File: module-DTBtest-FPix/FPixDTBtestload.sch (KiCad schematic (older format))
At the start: 11 parts, among them J1 CONN-SMK20, P15 RTD+, P16 RTD-

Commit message: Cleaned up the schematic, recovered from a non-present rescue library. Exported the netlist
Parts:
- R1, R2, R3, R4, R5, R6, R7: symbol R-RESCUE-FPix2DTB_90deg_up -> R
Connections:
- wire segments 62 -> 72
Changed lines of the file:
@@
 EESchema Schematic File Version 2
-LIBS:FPix2DTB_90deg_up-rescue
 LIBS:power
 LIBS:device
@@
 LIBS:contrib
 LIBS:valves
-LIBS:conn-scsi68
 LIBS:FPixDTBtestload-cache
 EELAYER 25 0
@@
 NoConn ~ 6400 4750
 $Comp
-L R-RESCUE-FPix2DTB_90deg_up R2
+L R R2
 U 1 1 526C35D1
 P 7750 2000
@@
 $EndComp
 $Comp
-L R-RESCUE-FPix2DTB_90deg_up R1
+L R R1
 U 1 1 526C35EF
 P 7750 1350
@@
 Jumper will short accross \nextra calibration resistor
 $Comp
-L R-RESCUE-FPix2DTB_90deg_up R3
+L R R3
 U 1 1 558082B2
 P 8100 4650
@@
 $EndComp
 $Comp
-L R-RESCUE-FPix2DTB_90deg_up R6
+L R R6
 U 1 1 5582CB84
 P 7700 5550
@@
 Connection ~ 8950 1650
 Connection ~ 8950 2300
-Wire Wire Line
-	7750 2300 7750 2250
 Connection ~ 8700 2300
 Connection ~ 7750 2300
@@
 	6400 4550 6650 4550
 Wire Wire Line
-	6400 4650 7850 4650
+	6400 4650 7950 4650
 Wire Wire Line
 	6400 4850 6650 4850
@@
 	7150 1100 7750 1100
 Wire Wire Line
-	7750 1600 7750 1750
-Wire Wire Line
 	7150 2300 8700 2300
 Wire Wire Line
@@
 	5650 5800 8100 5800
 $Comp
-L R-RESCUE-FPix2DTB_90deg_up R4
+L R R4
 U 1 1 5582CE8F
 P 7700 3650
@@
 Connection ~ 5650 3400
 $Comp
-L R-RESCUE-FPix2DTB_90deg_up R5
+L R R5
 U 1 1 5582D226
 P 8100 3650
@@
 Connection ~ 7700 3900
 $Comp
-L R-RESCUE-FPix2DTB_90deg_up R7
+L R R7
 U 1 1 5582D3F6
 P 8100 5550
@@
 	8350 6000 5650 6000
 Connection ~ 5650 6000
+Wire Wire Line
+	7750 1100 7750 1200
+Wire Wire Line
+	7750 1500 7750 1850
+Wire Wire Line
+	7750 2300 7750 2150
+Wire Wire Line
+	7700 3500 7700 3400
+Wire Wire Line
+	8100 3400 8100 3500
+Wire Wire Line
+	7700 3900 7700 3800
+Wire Wire Line
+	8100 3900 8100 3800
+Wire Wire Line
+	7700 5400 7700 5300
+Wire Wire Line
+	8100 5300 8100 5400
+Wire Wire Line
+	7700 5800 7700 5700
+Wire Wire Line
+	8100 5800 8100 5700
+Wire Wire Line
+	8250 4650 8350 4650
 $EndSCHEMATC

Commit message: Still working on getting the netlist operational
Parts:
- JP1: footprint Short_Link -> PIN_ARRAY_2X1
- R1, R2: footprint SM0603 -> Resistors_SMD:R_0603_HandSoldering
- R3: footprint (none) -> Resistors_SMD:R_Caddock_USF371
- R4, R5, R6, R7: footprint (none) -> Resistors_SMD:R_2512_HandSoldering
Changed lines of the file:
@@
 F 0 "R2" V 7830 2000 40  0000 C CNN
 F 1 "10k 0.1%" V 7757 2001 40  0000 C CNN
-F 2 "SM0603" V 7680 2000 30  0000 C CNN
+F 2 "Resistors_SMD:R_0603_HandSoldering" V 7680 2000 30  0000 C CNN
 F 3 "" H 7750 2000 30  0000 C CNN
 	1    7750 2000
@@
 F 0 "R1" V 7830 1350 40  0000 C CNN
 F 1 "10k 0.1%" V 7757 1351 40  0000 C CNN
-F 2 "SM0603" V 7680 1350 30  0000 C CNN
+F 2 "Resistors_SMD:R_0603_HandSoldering" V 7680 1350 30  0000 C CNN
 F 3 "" H 7750 1350 30  0000 C CNN
 	1    7750 1350
@@
 F 0 "JP1" H 8700 2150 60  0000 C CNN
 F 1 "JUMPER" H 8700 1920 40  0000 C CNN
-F 2 "Short_Link" H 8950 1800 60  0000 R CNN
+F 2 "PIN_ARRAY_2X1" H 8950 1800 60  0000 R CNN
 F 3 "" H 8700 2000 60  0000 C CNN
 	1    8700 2000
@@
 F 0 "R3" V 8180 4650 50  0000 C CNN
 F 1 "25 MEG" V 8107 4651 50  0000 C CNN
-F 2 "" V 8030 4650 30  0000 C CNN
+F 2 "Resistors_SMD:R_Caddock_USF371" V 8030 4650 30  0000 C CNN
 F 3 "" H 8100 4650 30  0000 C CNN
 	1    8100 4650
@@
 F 0 "R6" V 7780 5550 50  0000 C CNN
 F 1 "4.8" V 7707 5551 50  0000 C CNN
-F 2 "" V 7630 5550 30  0000 C CNN
+F 2 "Resistors_SMD:R_2512_HandSoldering" V 7630 5550 30  0000 C CNN
 F 3 "" H 7700 5550 30  0000 C CNN
 	1    7700 5550
@@
 F 0 "R4" V 7800 3650 50  0000 C CNN
 F 1 "3.2" V 7707 3651 50  0000 C CNN
-F 2 "" V 7630 3650 30  0000 C CNN
+F 2 "Resistors_SMD:R_2512_HandSoldering" V 7630 3650 30  0000 C CNN
 F 3 "" H 7700 3650 30  0000 C CNN
 	1    7700 3650
 	1    0    0    -1
 $EndComp
-Wire Wire Line
-	5650 3400 8100 3400
 Connection ~ 5650 5800
 Connection ~ 5650 3400
@@
 F 0 "R5" V 8180 3650 50  0000 C CNN
 F 1 "3.2" V 8107 3651 50  0000 C CNN
-F 2 "" V 8030 3650 30  0000 C CNN
+F 2 "Resistors_SMD:R_2512_HandSoldering" V 8030 3650 30  0000 C CNN
 F 3 "" H 8100 3650 30  0000 C CNN
 	1    8100 3650
 	1    0    0    -1
 $EndComp
-Connection ~ 7700 3400
 Connection ~ 7700 3900
 $Comp
@@
 F 0 "R7" V 8180 5550 50  0000 C CNN
 F 1 "4.8" V 8107 5551 50  0000 C CNN
-F 2 "" V 8030 5550 30  0000 C CNN
+F 2 "Resistors_SMD:R_2512_HandSoldering" V 8030 5550 30  0000 C CNN
 F 3 "" H 8100 5550 30  0000 C CNN
 	1    8100 5550
@@
 Wire Wire Line
 	8250 4650 8350 4650
+$Comp
+L GND #PWR?
+U 1 1 5584283A
+P 8500 3400
+F 0 "#PWR?" H 8500 3150 50  0001 C CNN
+F 1 "GND" H 8500 3250 50  0000 C CNN
+F 2 "" H 8500 3400 60  0000 C CNN
+F 3 "" H 8500 3400 60  0000 C CNN
+	1    8500 3400
+	1    0    0    -1
+$EndComp
+Wire Wire Line
+	7700 3400 8500 3400
+Connection ~ 8100 3400
 $EndSCHEMATC

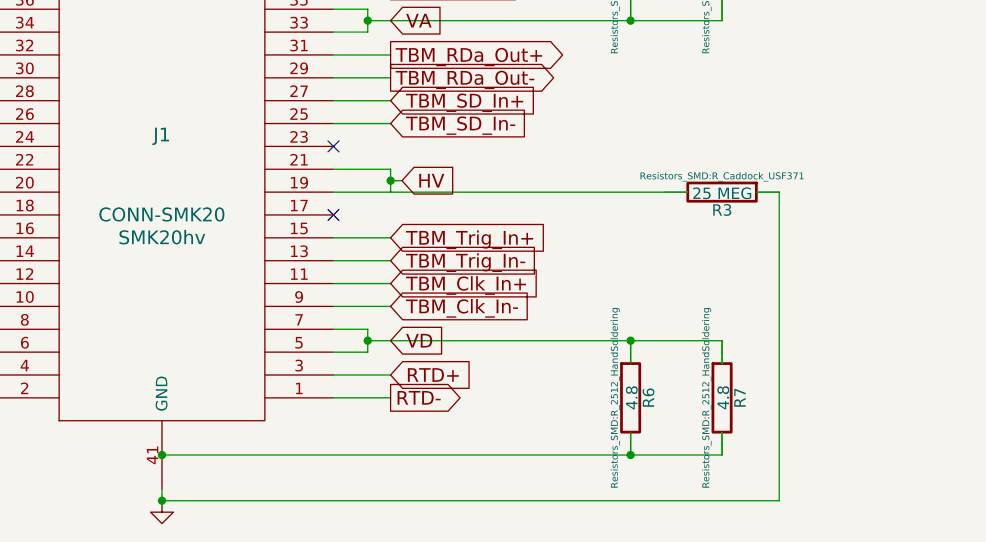
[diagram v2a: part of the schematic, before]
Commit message: Improved grounding
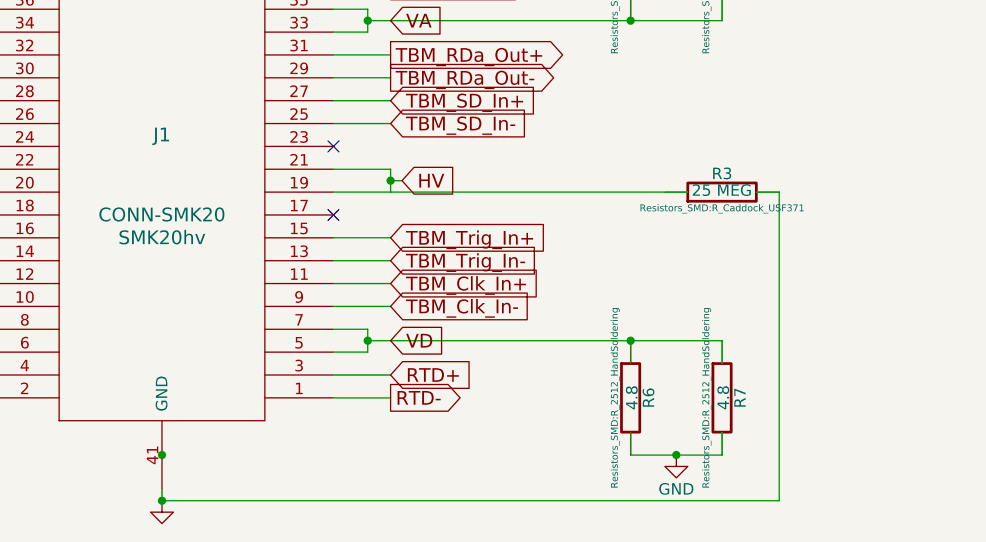
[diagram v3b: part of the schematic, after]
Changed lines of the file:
@@
 F 3 "" H 8100 4650 30  0000 C CNN
 	1    8100 4650
-	0    1    1    0
+	0    -1   -1   0
 $EndComp
 $Comp
@@
 	8700 1700 7750 1700
 Connection ~ 7750 1700
-Wire Wire Line
-	5650 5800 8100 5800
 $Comp
 L R R4
@@
 $EndComp
 Connection ~ 7700 5300
-Connection ~ 7700 5800
 $Comp
 L CONN-SMK20 J1
@@
 	8250 4650 8350 4650
 $Comp
-L GND #PWR?
+L GND #PWR06
 U 1 1 5584283A
 P 8500 3400
-F 0 "#PWR?" H 8500 3150 50  0001 C CNN
+F 0 "#PWR06" H 8500 3150 50  0001 C CNN
 F 1 "GND" H 8500 3250 50  0000 C CNN
 F 2 "" H 8500 3400 60  0000 C CNN
@@
 	7700 3400 8500 3400
 Connection ~ 8100 3400
+$Comp
+L GND #PWR?
+U 1 1 55842B75
+P 7900 5800
+F 0 "#PWR?" H 7900 5550 50  0001 C CNN
+F 1 "GND" H 7900 5650 50  0000 C CNN
+F 2 "" H 7900 5800 60  0000 C CNN
+F 3 "" H 7900 5800 60  0000 C CNN
+	1    7900 5800
+	1    0    0    -1
+$EndComp
+Wire Wire Line
+	7700 5800 8100 5800
+Connection ~ 7900 5800
 $EndSCHEMATC

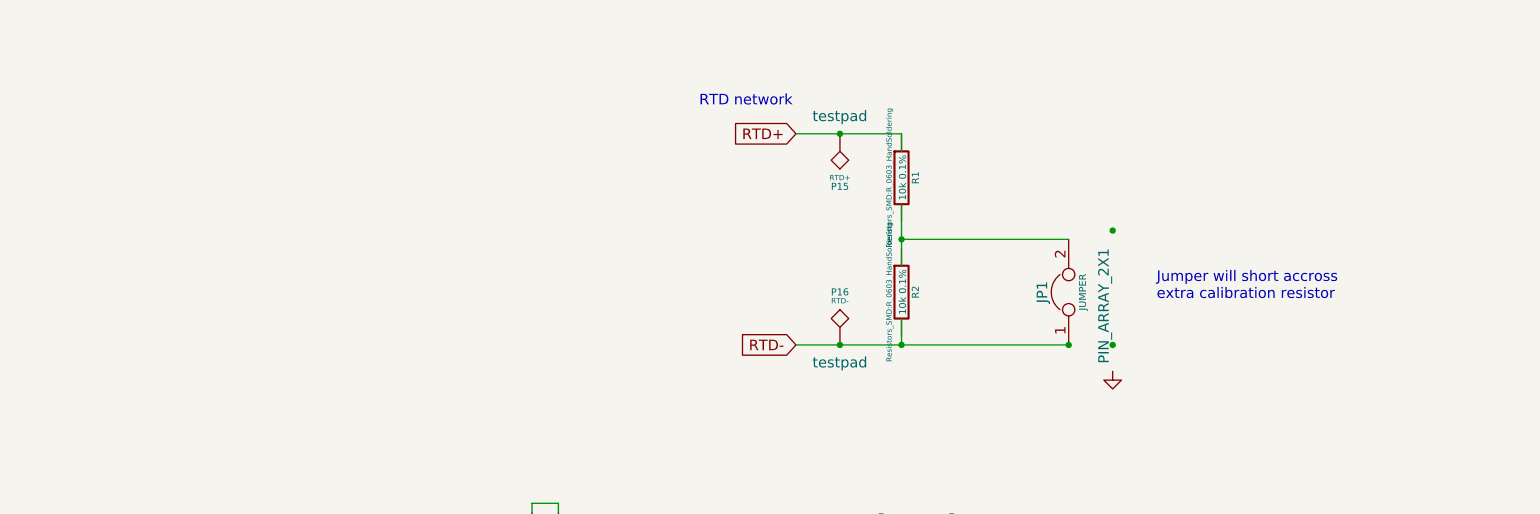
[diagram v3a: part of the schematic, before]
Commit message: Enhanced capabilities of resistor network. Now able to choose 0°C, -25°C and +25°C. Cleaned up GND jumper.
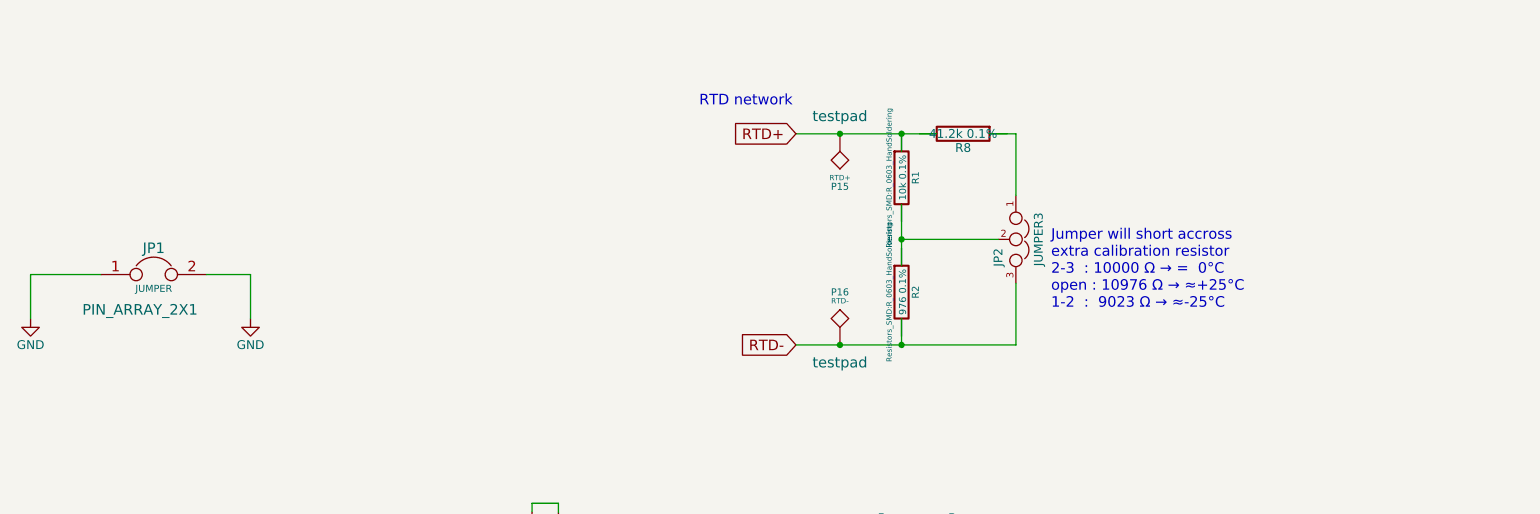
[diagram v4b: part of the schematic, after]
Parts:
- added JP2: JUMPER3, symbol JUMPER3
- added R8: 41.2k 0.1%, symbol R
- R2: value 10k 0.1% -> 976 0.1%
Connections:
- wire segments 72 -> 79
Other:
- note added: "Jumper will short accross \nextra calibration resistor\n2-3 : 10000 Ω → = 0°C\nopen : 10976 Ω → ≈+25°C\n1-2 : 9023 Ω → ≈-25°C"
- note removed: "Jumper will short accross \nextra calibration resistor"
- moved on the sheet: JP1
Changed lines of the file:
@@
 $EndDescr
 $Comp
-L GND #PWR01
+L GND #PWR8
 U 1 1 526C1DE7
 P 13700 -6750
-F 0 "#PWR01" H 13700 -6750 30  0001 C CNN
+F 0 "#PWR8" H 13700 -6750 30  0001 C CNN
 F 1 "GND" H 13700 -6820 30  0001 C CNN
 F 2 "" H 13700 -6750 60  0000 C CNN
@@
 VD
 $Comp
-L GND #PWR02
+L GND #PWR3
 U 1 1 526C1ECD
 P 4150 5650
-F 0 "#PWR02" H 4150 5650 30  0001 C CNN
+F 0 "#PWR3" H 4150 5650 30  0001 C CNN
 F 1 "GND" H 4150 5580 30  0001 C CNN
 F 2 "" H 4150 5650 60  0000 C CNN
@@
 P 7750 2000
 F 0 "R2" V 7830 2000 40  0000 C CNN
-F 1 "10k 0.1%" V 7757 2001 40  0000 C CNN
+F 1 "976 0.1%" V 7757 2001 40  0000 C CNN
 F 2 "Resistors_SMD:R_0603_HandSoldering" V 7680 2000 30  0000 C CNN
 F 3 "" H 7750 2000 30  0000 C CNN
@@
 RTD+
 $Comp
-L GND #PWR03
-U 1 1 526C8E08
-P 8950 2450
-F 0 "#PWR03" H 8950 2450 30  0001 C CNN
-F 1 "GND" H 8950 2380 30  0001 C CNN
-F 2 "" H 8950 2450 60  0000 C CNN
-F 3 "" H 8950 2450 60  0000 C CNN
-	1    8950 2450
-	1    0    0    -1
-$EndComp
-$Comp
 L JUMPER JP1
 U 1 1 526EC969
-P 8700 2000
-F 0 "JP1" H 8700 2150 60  0000 C CNN
-F 1 "JUMPER" H 8700 1920 40  0000 C CNN
-F 2 "PIN_ARRAY_2X1" H 8950 1800 60  0000 R CNN
-F 3 "" H 8700 2000 60  0000 C CNN
-	1    8700 2000
-	0    -1   -1   0
+P 3500 1900
+F 0 "JP1" H 3500 2050 60  0000 C CNN
+F 1 "JUMPER" H 3500 1820 40  0000 C CNN
+F 2 "PIN_ARRAY_2X1" H 3750 1700 60  0000 R CNN
+F 3 "" H 3500 1900 60  0000 C CNN
+	1    3500 1900
+	1    0    0    -1
 $EndComp
 $Comp
@@
 VA
 $Comp
-L GND #PWR04
+L GND #PWR4
 U 1 1 52840820
 P 5650 6000
-F 0 "#PWR04" H 5650 6000 30  0001 C CNN
+F 0 "#PWR4" H 5650 6000 30  0001 C CNN
 F 1 "GND" H 5650 5930 30  0001 C CNN
 F 2 "" H 5650 6000 60  0000 C CNN
@@
 $EndComp
 $Comp
-L GND #PWR05
+L GND #PWR5
 U 1 1 52840925
 P 5800 3250
-F 0 "#PWR05" H 5800 3250 30  0001 C CNN
+F 0 "#PWR5" H 5800 3250 30  0001 C CNN
 F 1 "GND" H 5800 3180 30  0001 C CNN
 F 2 "" H 5800 3250 60  0000 C CNN
@@
 Text Notes 6600 950  0    60   ~ 0
 RTD network
-Text Notes 9200 2050 0    60   ~ 0
-Jumper will short accross \nextra calibration resistor
+Text Notes 8600 2100 0    60   ~ 0
+Jumper will short accross \nextra calibration resistor\n2-3  : 10000 Ω → =  0°C\nopen : 10976 Ω → ≈+25°C\n1-2  :  9023 Ω → ≈-25°C
 $Comp
 L R R3
@@
 	1    0    0    -1
 $EndComp
-Connection ~ 8950 1650
-Connection ~ 8950 2300
-Connection ~ 8700 2300
 Connection ~ 7750 2300
 Connection ~ 7400 1100
@@
 	6400 5550 6650 5550
 Wire Wire Line
-	7150 1100 7750 1100
-Wire Wire Line
-	7150 2300 8700 2300
-Wire Wire Line
-	8700 1700 7750 1700
+	7150 1100 7950 1100
 Connection ~ 7750 1700
 $Comp
@@
 	8250 4650 8350 4650
 $Comp
-L GND #PWR06
+L GND #PWR7
 U 1 1 5584283A
 P 8500 3400
-F 0 "#PWR06" H 8500 3150 50  0001 C CNN
+F 0 "#PWR7" H 8500 3150 50  0001 C CNN
 F 1 "GND" H 8500 3250 50  0000 C CNN
 F 2 "" H 8500 3400 60  0000 C CNN
@@
 Connection ~ 8100 3400
 $Comp
-L GND #PWR?
+L GND #PWR6
 U 1 1 55842B75
 P 7900 5800
-F 0 "#PWR?" H 7900 5550 50  0001 C CNN
+F 0 "#PWR6" H 7900 5550 50  0001 C CNN
 F 1 "GND" H 7900 5650 50  0000 C CNN
 F 2 "" H 7900 5800 60  0000 C CNN
@@
 	7700 5800 8100 5800
 Connection ~ 7900 5800
+$Comp
+L GND #PWR1
+U 1 1 5584F80D
+P 2800 2150
+F 0 "#PWR1" H 2800 1900 50  0001 C CNN
+F 1 "GND" H 2800 2000 50  0000 C CNN
+F 2 "" H 2800 2150 60  0000 C CNN
+F 3 "" H 2800 2150 60  0000 C CNN
+	1    2800 2150
+	1    0    0    -1
+$EndComp
+$Comp
+L GND #PWR2
+U 1 1 5584F842
+P 4050 2150
+F 0 "#PWR2" H 4050 1900 50  0001 C CNN
+F 1 "GND" H 4050 2000 50  0000 C CNN
+F 2 "" H 4050 2150 60  0000 C CNN
+F 3 "" H 4050 2150 60  0000 C CNN
+	1    4050 2150
+	1    0    0    -1
+$EndComp
+Wire Wire Line
+	2800 2150 2800 1900
+Wire Wire Line
+	2800 1900 3200 1900
+Wire Wire Line
+	3800 1900 4050 1900
+Wire Wire Line
+	4050 1900 4050 2150
+$Comp
+L JUMPER3 JP2
+U 1 1 5584F9E1
+P 8400 1700
+F 0 "JP2" H 8450 1600 50  0000 L CNN
+F 1 "JUMPER3" H 8400 1800 50  0000 C BNN
+F 2 "" H 8400 1700 60  0000 C CNN
+F 3 "" H 8400 1700 60  0000 C CNN
+	1    8400 1700
+	0    1    1    0
+$EndComp
+Wire Wire Line
+	7750 1700 8300 1700
+Wire Wire Line
+	7150 2300 8400 2300
+Wire Wire Line
+	8400 2300 8400 1950
+$Comp
+L R R8
+U 1 1 5584FF1F
+P 8100 1100
+F 0 "R8" V 8180 1100 50  0000 C CNN
+F 1 "41.2k 0.1%" V 8100 1100 50  0000 C CNN
+F 2 "" V 8030 1100 30  0000 C CNN
+F 3 "" H 8100 1100 30  0000 C CNN
+	1    8100 1100
+	0    1    1    0
+$EndComp
+Connection ~ 7750 1100
+Wire Wire Line
+	8250 1100 8400 1100
+Wire Wire Line
+	8400 1100 8400 1450
 $EndSCHEMATC

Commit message: Layout ok. TODO: rotate connector and re-layout everything...
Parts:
- JP2: footprint (none) -> Pin_Headers:Pin_Header_Straight_1x03
- R8: footprint (none) -> Resistors_SMD:R_0603_HandSoldering
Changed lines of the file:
@@
 $EndDescr
 $Comp
-L GND #PWR8
+L GND #PWR01
 U 1 1 526C1DE7
 P 13700 -6750
-F 0 "#PWR8" H 13700 -6750 30  0001 C CNN
+F 0 "#PWR01" H 13700 -6750 30  0001 C CNN
 F 1 "GND" H 13700 -6820 30  0001 C CNN
 F 2 "" H 13700 -6750 60  0000 C CNN
@@
 VD
 $Comp
-L GND #PWR3
+L GND #PWR02
 U 1 1 526C1ECD
 P 4150 5650
-F 0 "#PWR3" H 4150 5650 30  0001 C CNN
+F 0 "#PWR02" H 4150 5650 30  0001 C CNN
 F 1 "GND" H 4150 5580 30  0001 C CNN
 F 2 "" H 4150 5650 60  0000 C CNN
@@
 VA
 $Comp
-L GND #PWR4
+L GND #PWR03
 U 1 1 52840820
 P 5650 6000
-F 0 "#PWR4" H 5650 6000 30  0001 C CNN
+F 0 "#PWR03" H 5650 6000 30  0001 C CNN
 F 1 "GND" H 5650 5930 30  0001 C CNN
 F 2 "" H 5650 6000 60  0000 C CNN
@@
 $EndComp
 $Comp
-L GND #PWR5
+L GND #PWR04
 U 1 1 52840925
 P 5800 3250
-F 0 "#PWR5" H 5800 3250 30  0001 C CNN
+F 0 "#PWR04" H 5800 3250 30  0001 C CNN
 F 1 "GND" H 5800 3180 30  0001 C CNN
 F 2 "" H 5800 3250 60  0000 C CNN
@@
 Connection ~ 7400 2300
 Wire Wire Line
-	6650 4550 6650 4650
-Wire Wire Line
 	6650 4600 6700 4600
 Connection ~ 6650 4600
@@
 	8250 4650 8350 4650
 $Comp
-L GND #PWR7
+L GND #PWR05
 U 1 1 5584283A
 P 8500 3400
-F 0 "#PWR7" H 8500 3150 50  0001 C CNN
+F 0 "#PWR05" H 8500 3150 50  0001 C CNN
 F 1 "GND" H 8500 3250 50  0000 C CNN
 F 2 "" H 8500 3400 60  0000 C CNN
@@
 Connection ~ 8100 3400
 $Comp
-L GND #PWR6
+L GND #PWR06
 U 1 1 55842B75
 P 7900 5800
-F 0 "#PWR6" H 7900 5550 50  0001 C CNN
+F 0 "#PWR06" H 7900 5550 50  0001 C CNN
 F 1 "GND" H 7900 5650 50  0000 C CNN
 F 2 "" H 7900 5800 60  0000 C CNN
@@
 Connection ~ 7900 5800
 $Comp
-L GND #PWR1
+L GND #PWR07
 U 1 1 5584F80D
 P 2800 2150
-F 0 "#PWR1" H 2800 1900 50  0001 C CNN
+F 0 "#PWR07" H 2800 1900 50  0001 C CNN
 F 1 "GND" H 2800 2000 50  0000 C CNN
 F 2 "" H 2800 2150 60  0000 C CNN
@@
 $EndComp
 $Comp
-L GND #PWR2
+L GND #PWR08
 U 1 1 5584F842
 P 4050 2150
-F 0 "#PWR2" H 4050 1900 50  0001 C CNN
+F 0 "#PWR08" H 4050 1900 50  0001 C CNN
 F 1 "GND" H 4050 2000 50  0000 C CNN
 F 2 "" H 4050 2150 60  0000 C CNN
@@
 F 0 "JP2" H 8450 1600 50  0000 L CNN
 F 1 "JUMPER3" H 8400 1800 50  0000 C BNN
-F 2 "" H 8400 1700 60  0000 C CNN
+F 2 "Pin_Headers:Pin_Header_Straight_1x03" H 8400 1700 60  0000 C CNN
 F 3 "" H 8400 1700 60  0000 C CNN
 	1    8400 1700
@@
 F 0 "R8" V 8180 1100 50  0000 C CNN
 F 1 "41.2k 0.1%" V 8100 1100 50  0000 C CNN
-F 2 "" V 8030 1100 30  0000 C CNN
+F 2 "Resistors_SMD:R_0603_HandSoldering" V 8030 1100 30  0000 C CNN
 F 3 "" H 8100 1100 30  0000 C CNN
 	1    8100 1100
@@
 Wire Wire Line
 	8400 1100 8400 1450
+Wire Wire Line
+	6650 4550 6650 4650
+Connection ~ 6650 4650
 $EndSCHEMATC
